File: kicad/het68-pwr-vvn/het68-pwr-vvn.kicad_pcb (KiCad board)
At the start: 2 copper layers, 140 x 80 mm, 64 parts, among them J1 CT_SEC, J2 USB_C, J3 VOUT, Q1 X0202MN

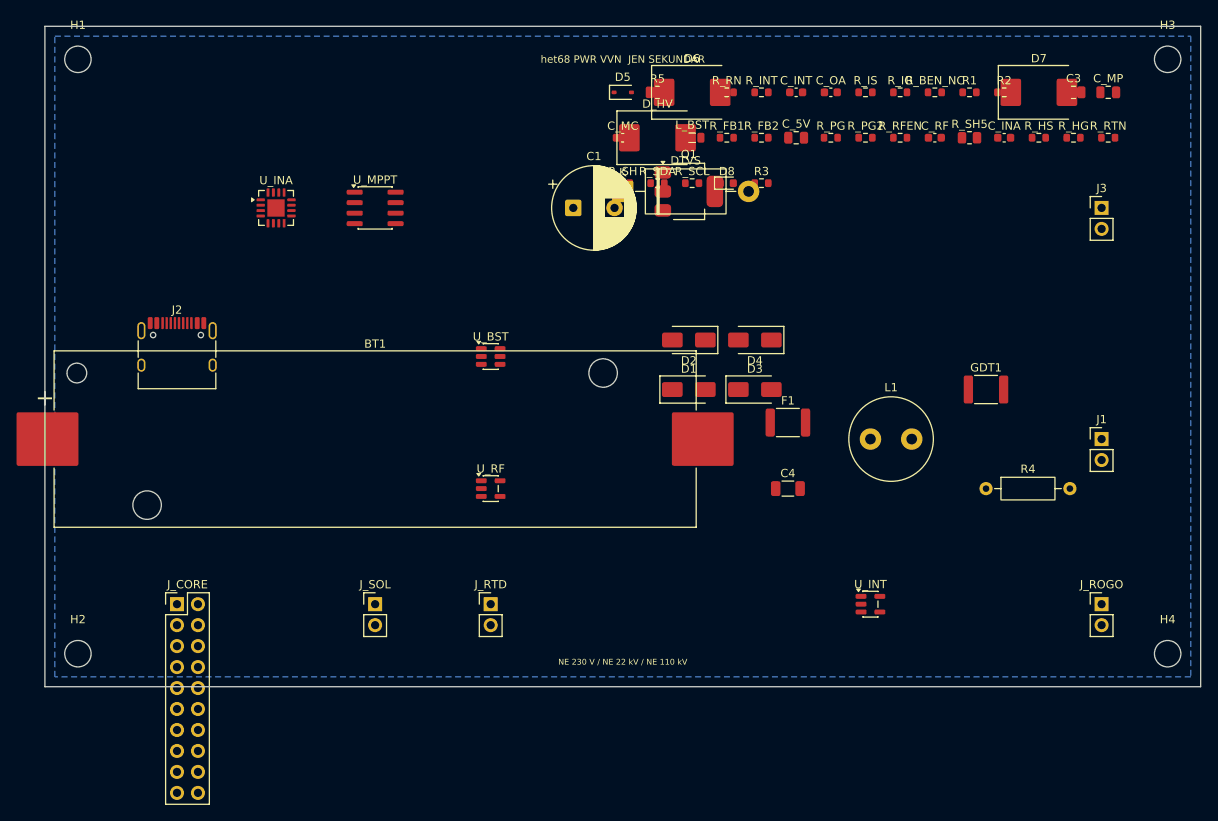
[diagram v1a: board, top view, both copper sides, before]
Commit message: Add a Core status LED and three buttons, and fit a 21700 holder.
RESET, BOOT and USER sit on the east edge with one SK6812; the power board uses a Keystone 1122 instead of an 18650 sled. Masks, schematics and JLCPCB gerber zips are in the tree.

Co-authored-by: Cursor <cursoragent@cursor.com>
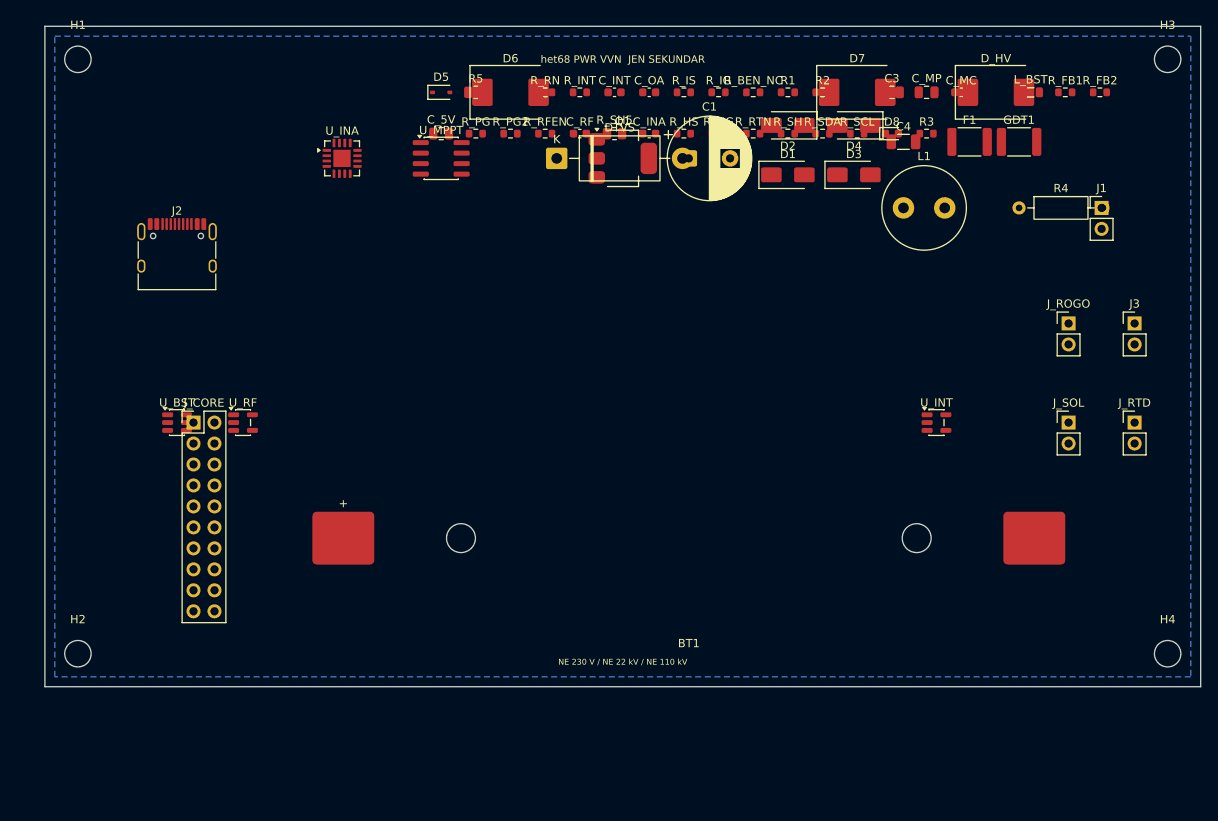
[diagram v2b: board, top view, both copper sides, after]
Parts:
- BT1: value LiFePO4_1S -> 21700; footprint Battery:BatteryHolder_Keystone_1042_1x18650 -> het68:Keystone_1122_21700
- moved J_SOL 86.8 mm to (124.0, 48.0)
- moved J_RTD 81.0 mm to (132.0, 48.0)
- moved C4 44.3 mm to (104.0, 14.0)
- moved R_RTN 43.0 mm to (85.8, 13.0)
- moved R_PG2 43.0 mm to (56.4, 13.0)
- moved C_5V 43.0 mm to (48.0, 13.0)
- moved C_INA 43.0 mm to (73.2, 13.0)
- moved C_RF 43.0 mm to (64.8, 13.0)
- moved R_HG 43.0 mm to (81.6, 13.0)
- moved R_HS 43.0 mm to (77.4, 13.0)
- moved R_PG 43.0 mm to (52.2, 13.0)
- moved R_SH5 43.0 mm to (69.0, 13.0)
- moved R_RFEN 43.0 mm to (60.6, 13.0)
- moved C_MC 41.4 mm to (111.0, 8.00)
- moved D_HV 41.4 mm to (115.2, 8.00)
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
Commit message: Route signal copper on the five v4 boards and drop tracks that still short.
Core and the satellite have no copper shorts left. QFN-80 fanout and a few LVDS pairs stay open, and the power boards still have overlapping pads from placement.

Co-authored-by: Cursor <cursoragent@cursor.com>
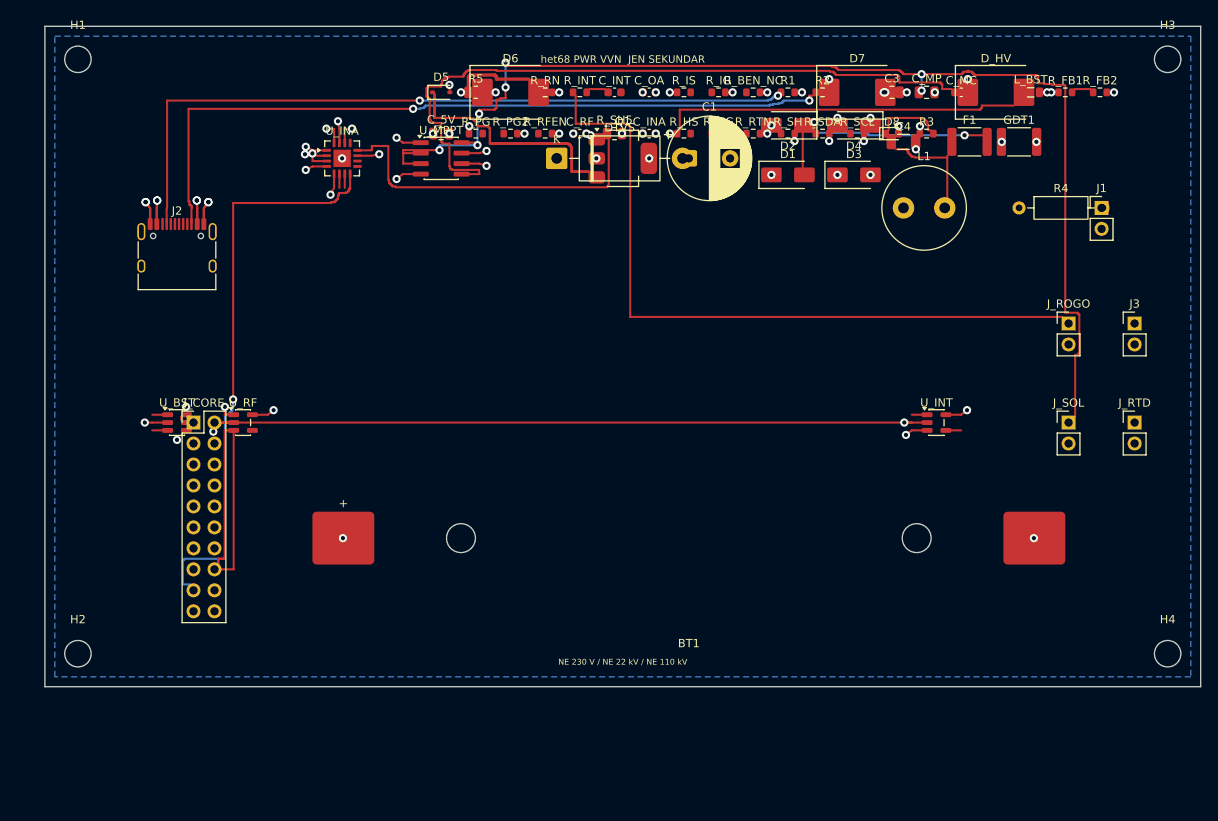
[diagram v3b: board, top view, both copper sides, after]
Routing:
- net SOL_P: track 0.00 -> 148.3 mm, vias 0 -> 7
- net GND: track 0.00 -> 134.3 mm, vias 0 -> 36
- net CC2: track 0.00 -> 92.2 mm, vias 0 -> 2
- net CC1: track 0.00 -> 90.2 mm, vias 0 -> 2
- net MPPT_C: track 0.00 -> 87.4 mm
- net ROGO_P: track 0.00 -> 86.7 mm
- net I2C0_ALERT: track 0.00 -> 72.3 mm, vias 0 -> 1
- net SCR_G: track 0.00 -> 58.2 mm
- net EN_RF: track 0.00 -> 55.6 mm
- net VHARV: track 0.00 -> 47.0 mm, vias 0 -> 3
- net 5V_IN: track 0.00 -> 41.7 mm
- net AC1F: track 0.00 -> 28.8 mm, vias 0 -> 2
- net AC1L: track 0.00 -> 15.7 mm
- net DC: track 0.00 -> 13.6 mm, vias 0 -> 7
- net VBUS: track 0.00 -> 11.4 mm, vias 0 -> 6
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
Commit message: Fan out the RP2350B and finish the signal bridges that can leave the package.
Each QFN pin gets a 0.15 mm escape along its axis. The crystal moves off the north row so that corridor exists. Core and the satellite have no new shorts; a few center-row pins and some LVDS nets are still open.

Co-authored-by: Cursor <cursoragent@cursor.com>
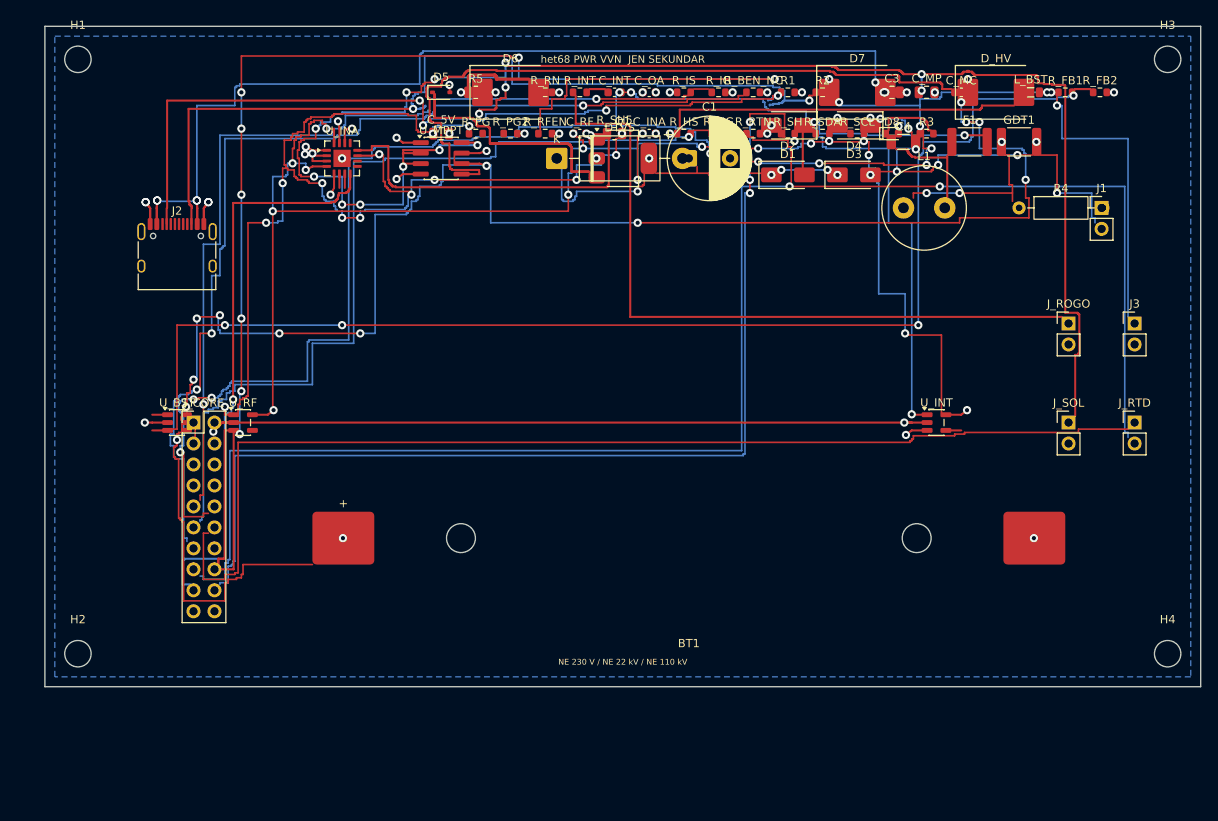
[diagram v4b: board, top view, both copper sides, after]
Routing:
- net +5V_ALWAYS: track 8.25 -> 256.9 mm, vias 10 -> 26
- net BAT: track 6.53 -> 217.1 mm, vias 6 -> 16
- net PT1000_RTN: track 1.39 -> 203.4 mm, vias 0 -> 2
- net ADC_ROGO: track 3.25 -> 186.7 mm, vias 0 -> 6
- net +3V3_RF: track 10.8 -> 190.4 mm, vias 9 -> 19
- net BST_FB: track 6.74 -> 156.3 mm, vias 0 -> 4
- net EN_RF: track 55.6 -> 204.0 mm, vias 0 -> 8
- net ADC_PT1000: track 1.39 -> 137.8 mm
- net SHIELD: track 1.39 -> 129.8 mm, vias 0 -> 3
- net BURDEN_EN: track 1.39 -> 126.8 mm, vias 0 -> 3
- net ADC_I: track 1.39 -> 111.4 mm, vias 0 -> 2
- net VBUS: track 11.4 -> 120.4 mm, vias 6 -> 7
- net ADC_HARVEST: track 1.39 -> 109.0 mm, vias 0 -> 1
- net SOL_P: track 148.3 -> 202.9 mm, vias 7 -> 14
- net AC2: track 1.80 -> 48.0 mm, vias 4 -> 10
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
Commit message: Put the satellite electronics on the back and clear the power-board pad shorts.
The outward face keeps only the microphone hole and the eight SK6812s. The DO-201 and the two regulators move off the header so the power boards no longer short pad to pad. Some LVDS, QSPI and GPIO nets are still open.

Co-authored-by: Cursor <cursoragent@cursor.com>
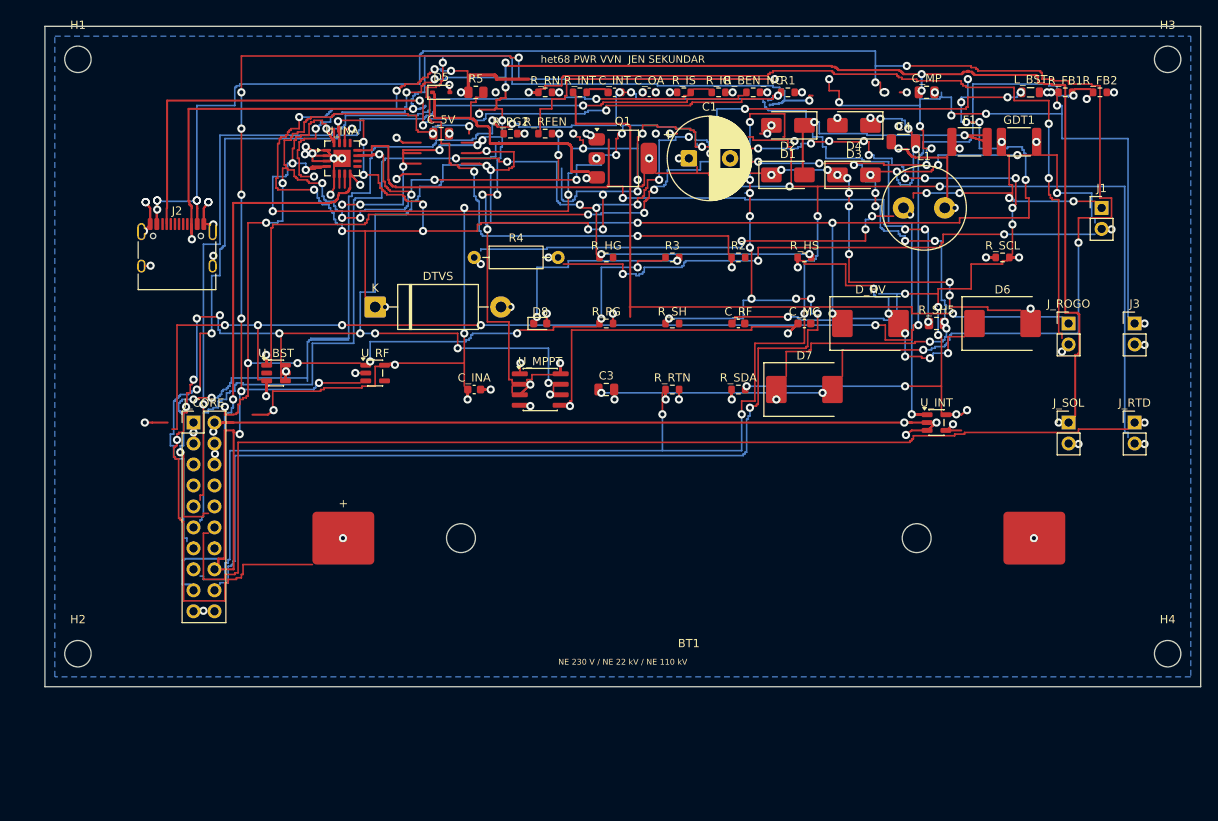
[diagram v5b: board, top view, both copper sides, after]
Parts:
- moved R4 66.3 mm to (52.0, 28.0)
- moved D6 65.8 mm to (116.0, 36.0)
- moved C3 49.9 mm to (68.0, 44.0)
- moved D8 48.4 mm to (60.0, 36.0)
- moved R_SH5 45.3 mm to (108.0, 36.0)
- moved C_INA 37.6 mm to (52.0, 44.0)
- moved D7 36.6 mm to (92.0, 44.0)
- moved R3 34.3 mm to (76.0, 28.0)
- moved C_MC 33.8 mm to (92.0, 36.0)
- moved R_SDA 32.6 mm to (84.0, 44.0)
- moved R_RTN 32.5 mm to (76.0, 44.0)
- moved D_HV 31.9 mm to (100.0, 36.0)
- moved U_MPPT 30.5 mm to (60.0, 44.0)
- moved C_RF 30.0 mm to (84.0, 36.0)
- moved DTVS 28.4 mm to (40.0, 34.0)
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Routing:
- net VBUS: track 120.4 -> 305.3 mm, vias 7 -> 13
- net DC: track 50.6 -> 229.1 mm, vias 10 -> 32
- net +3V3_RF: track 190.4 -> 352.9 mm, vias 19 -> 35
- net +5V_ALWAYS: track 256.9 -> 407.9 mm, vias 26 -> 46
- net BST_SW: track 1.86 -> 132.4 mm, vias 0 -> 7
- net GND: track 133.4 -> 246.7 mm, vias 36 -> 54
- net ROGO_N: track 1.39 -> 108.6 mm, vias 0 -> 4
- net CC2: track 107.7 -> 190.9 mm, vias 2 -> 7
- net AC2: track 48.0 -> 124.4 mm, vias 10 -> 15
- net BAT: track 217.1 -> 286.7 mm, vias 16 -> 24
- net AC1: track 19.0 -> 86.7 mm, vias 3 -> 10
- net SOL_P: track 202.9 -> 266.5 mm, vias 14 -> 22
- net 5V_IN: track 41.7 -> 96.9 mm, vias 0 -> 4
- net ADC_HARVEST: track 109.0 -> 157.6 mm, vias 1 -> 9
- net MPPT_C: track 87.4 -> 49.9 mm, vias 0 -> 2
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
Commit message: Ship the furthest routed v4 boards with matching previews.
The satellite signal nets are closed, the five boards have no shorts, and the gerbers and renders follow this copper.

Co-authored-by: Cursor <cursoragent@cursor.com>
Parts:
- moved J_SOL 2.95 mm to (127.0, 48.0)
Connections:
- J2 pad A6: unconnected-(J2-D+-PadA6) -> (no net)
- J2 pad A7: unconnected-(J2-D--PadA7) -> (no net)
- J2 pad A8: unconnected-(J2-SBU1-PadA8) -> (no net)
- J2 pad B6: unconnected-(J2-D+-PadB6) -> (no net)
- J2 pad B7: unconnected-(J2-D--PadB7) -> (no net)
- J2 pad B8: unconnected-(J2-SBU2-PadB8) -> (no net)
- U_INA pad 10: unconnected-(U_INA-PV-Pad10) -> (no net)
- U_INA pad 13: unconnected-(U_INA-TC-Pad13) -> (no net)
- U_INA pad 9: unconnected-(U_INA-CRITICAL-Pad9) -> (no net)
- U_RF pad 4: unconnected-(U_RF-NC-Pad4) -> (no net)
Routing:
- net GND: track 246.7 -> 556.1 mm, vias 54 -> 64
- net AC2: track 124.4 -> 138.8 mm
- net SOL_P: track 266.5 -> 277.7 mm
- net AC1: track 86.7 -> 93.9 mm, vias 10 -> 11
- net PT1000_RTN: track 229.2 -> 231.9 mm
- net ADC_PT1000: track 139.0 -> 141.3 mm
- net ADC_I: track 111.8 -> 113.4 mm
- net ROGO_N: track 108.6 -> 110.2 mm
- net BURDEN_EN: track 126.8 -> 128.3 mm, vias 3 -> 4
- net DC: track 229.1 -> 230.5 mm
- net ADC_HARVEST: track 157.6 -> 158.8 mm, vias 9 -> 10
- net SHIELD: track 159.8 -> 160.9 mm, vias 11 -> 12
- net ADC_ROGO: track 205.2 -> 206.4 mm
